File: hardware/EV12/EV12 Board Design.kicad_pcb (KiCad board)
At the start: 4 copper layers, 66 x 99.3 mm, 132 parts, among them CN2 Conn_05x02_Female, CN3 Conn_01x06_Female, CN4 Conn_01x06_Female, CN5 Conn_02x05_Male, CN6 Conn_02x05_Male, CN7 Conn_02x05_Male, J1 Conn_01x02_Socket, J10 Conn_01x08_Socket, J2 AudioJack1, J3 Conn_01x06_Socket, J9 USB_C_Receptacle, Q1 SS8050, Q2 SS8050, SW1 TS-1037-A11B3-D2, SW3 TS-1037-A11B3-D2, SW4 SW_Push, SW5 SW_Push, SW6 SW_SPDT, U1 STM32F405RGTx, U11 ESP32-S3-WROOM-1-N8R2, U13 BM14B(0.8)-24DS-0.4V(53), U2 BQ21040DBV, U3 CH340C, U4 USBLC6-2P6, U5 M24C02-RMN6TP, U6 WM8960CGEFL/RV, U7 TPS63060, U8 STM32F072CBTx, Y1 Crystal_GND24

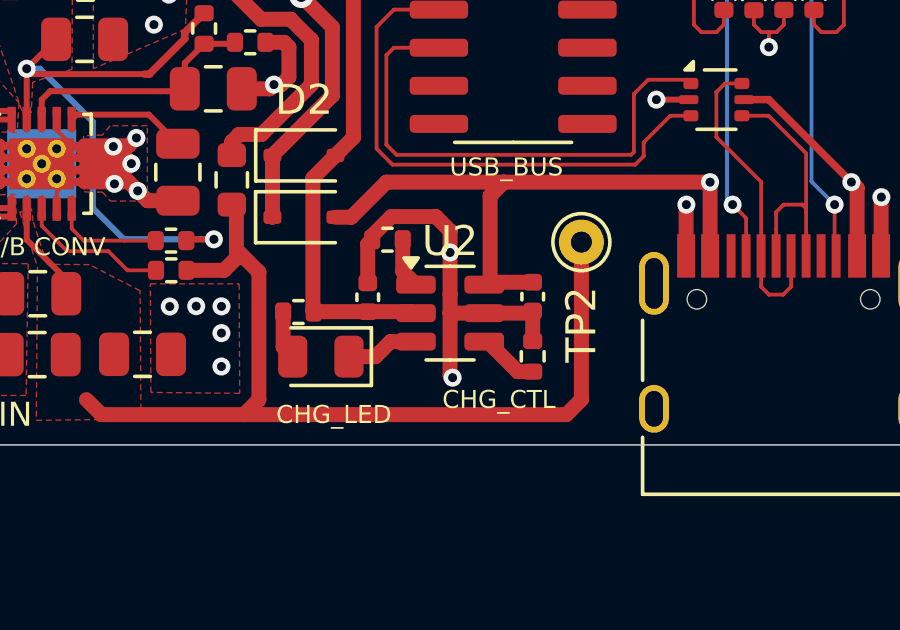
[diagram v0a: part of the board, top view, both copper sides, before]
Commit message: Added missing capacitor to BQ21040DVR battery charger
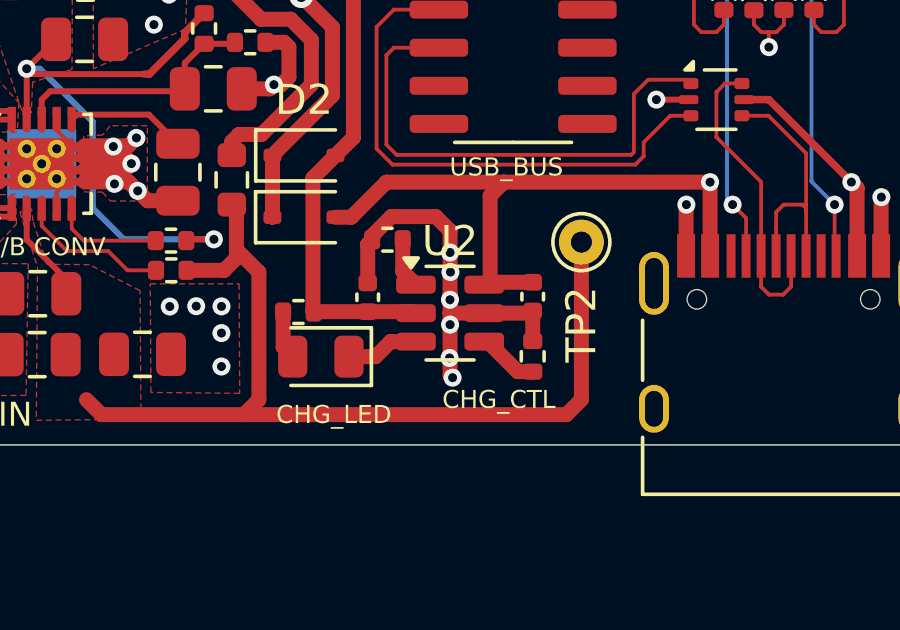
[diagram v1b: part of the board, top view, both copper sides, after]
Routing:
- net GND: vias 71 -> 75
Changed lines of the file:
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@@
 		(tags "resistor")
 		(property "Reference" "R43"
-			(at 0 -1.17 360)
+			(at 0 -1.17 0)
 			(layer "F.SilkS")
 			(hide yes)
@@
 		)
 		(property "Value" "10k"
-			(at 0 1.17 360)
+			(at 0 1.17 0)
 			(layer "F.Fab")
 			(effects
@@
 		)
 		(fp_text user "${REFERENCE}"
-			(at 0 0 360)
+			(at 0 0 0)
 			(layer "F.Fab")
 			(effects
@@
 		(tags "SOT TO_SOT_SMD")
 		(property "Reference" "Q1"
-			(at 0 -2.4 360)
+			(at 0 -2.4 0)
 			(layer "F.SilkS")
 			(hide yes)
@@
 		)
 		(property "Value" "SS8050"
-			(at 0 2.4 360)
+			(at 0 2.4 0)
 			(layer "F.Fab")
 			(effects
@@
 		)
 		(fp_text user "${REFERENCE}"
-			(at 0 0 360)
+			(at 0 0 0)
 			(layer "F.Fab")
 			(effects
@@
 		(tags "SOT TO_SOT_SMD")
 		(property "Reference" "Q2"
-			(at 0 -2.4 360)
+			(at 0 -2.4 0)
 			(layer "F.SilkS")
 			(effects
@@
 		)
 		(property "Value" "SS8050"
-			(at 0 2.4 360)
+			(at 0 2.4 0)
 			(layer "F.Fab")
 			(effects
@@
 		)
 		(fp_text user "${REFERENCE}"
-			(at 0 0 360)
+			(at 0 0 0)
 			(layer "F.Fab")
 			(effects
@@
 		(tags "resistor")
 		(property "Reference" "R28"
-			(at 0.01 0.75 360)
+			(at 0.01 0.75 0)
 			(layer "F.SilkS")
 			(hide yes)
@@
 		)
 		(property "Value" "1k0"
-			(at 0 1.17 360)
+			(at 0 1.17 0)
 			(layer "F.Fab")
 			(effects
@@
 		)
 		(property "Footprint" "Resistor_SMD:R_0402_1005Metric"
-			(at 0 0 360)
+			(at 0 0 0)
 			(layer "F.Fab")
 			(hide yes)
@@
 		)
 		(property "Datasheet" ""
-			(at 0 0 360)
+			(at 0 0 0)
 			(layer "F.Fab")
 			(hide yes)
@@
 		)
 		(property "Description" "Resistor, US symbol"
-			(at 0 0 360)
+			(at 0 0 0)
 			(layer "F.Fab")
 			(hide yes)
@@
 		)
 		(fp_text user "${REFERENCE}"
-			(at 0 0 360)
+			(at 0 0 0)
 			(layer "F.Fab")
 			(effects
@@
 		(tags "resistor")
 		(property "Reference" "R44"
-			(at 0 -1.17 360)
+			(at 0 -1.17 0)
 			(layer "F.SilkS")
 			(hide yes)
@@
 		)
 		(property "Value" "10k"
-			(at 0 1.17 360)
+			(at 0 1.17 0)
 			(layer "F.Fab")
 			(effects
@@
 		)
 		(fp_text user "${REFERENCE}"
-			(at 0 0 360)
+			(at 0 0 0)
 			(layer "F.Fab")
 			(effects
@@
 	)
 	(via
+		(at 135.865743 142.400165)
+		(size 0.6)
+		(drill 0.3)
+		(layers "F.Cu" "B.Cu")
+		(free yes)
+		(net 4)
+	)
+	(via
 		(at 126.26 126.79)
 		(size 0.6)
@@
 	)
 	(via
+		(at 135.8825 141.29)
+		(size 0.6)
+		(drill 0.3)
+		(layers "F.Cu" "B.Cu")
+		(free yes)
+		(net 4)
+	)
+	(via
 		(at 124.657571 135.353492)
 		(size 0.6)
@@
 	)
 	(via
+		(at 135.879657 140.460748)
+		(size 0.6)
+		(drill 0.3)
+		(layers "F.Cu" "B.Cu")
+		(free yes)
+		(net 4)
+	)
+	(via
 		(at 170.76 102.04)
 		(size 0.6)
@@
 		(net 4)
 	)
+	(via
+		(at 135.894594 139.53812)
+		(size 0.6)
+		(drill 0.3)
+		(layers "F.Cu" "B.Cu")
+		(free yes)
+		(net 4)
+	)

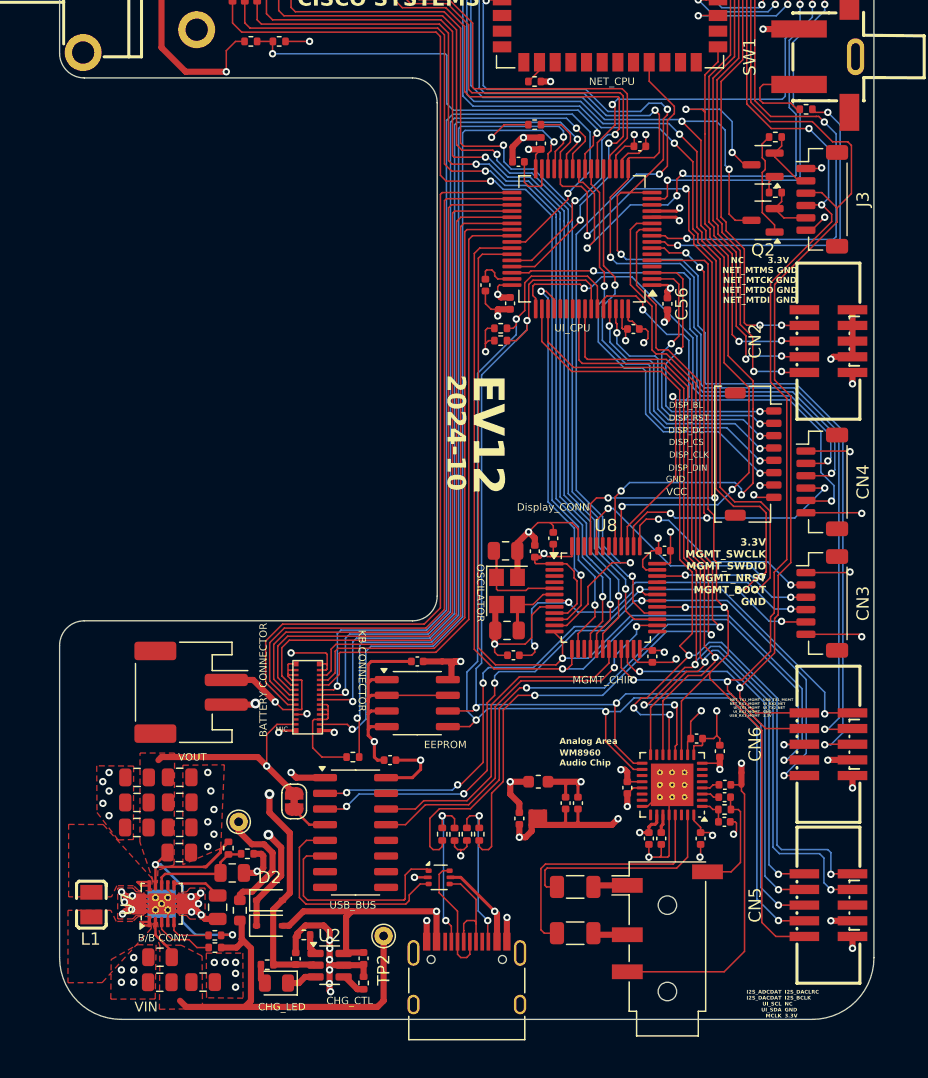
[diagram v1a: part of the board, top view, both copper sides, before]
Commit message: Moved keyboard conn, eeprom, and battery connector. Added diodes
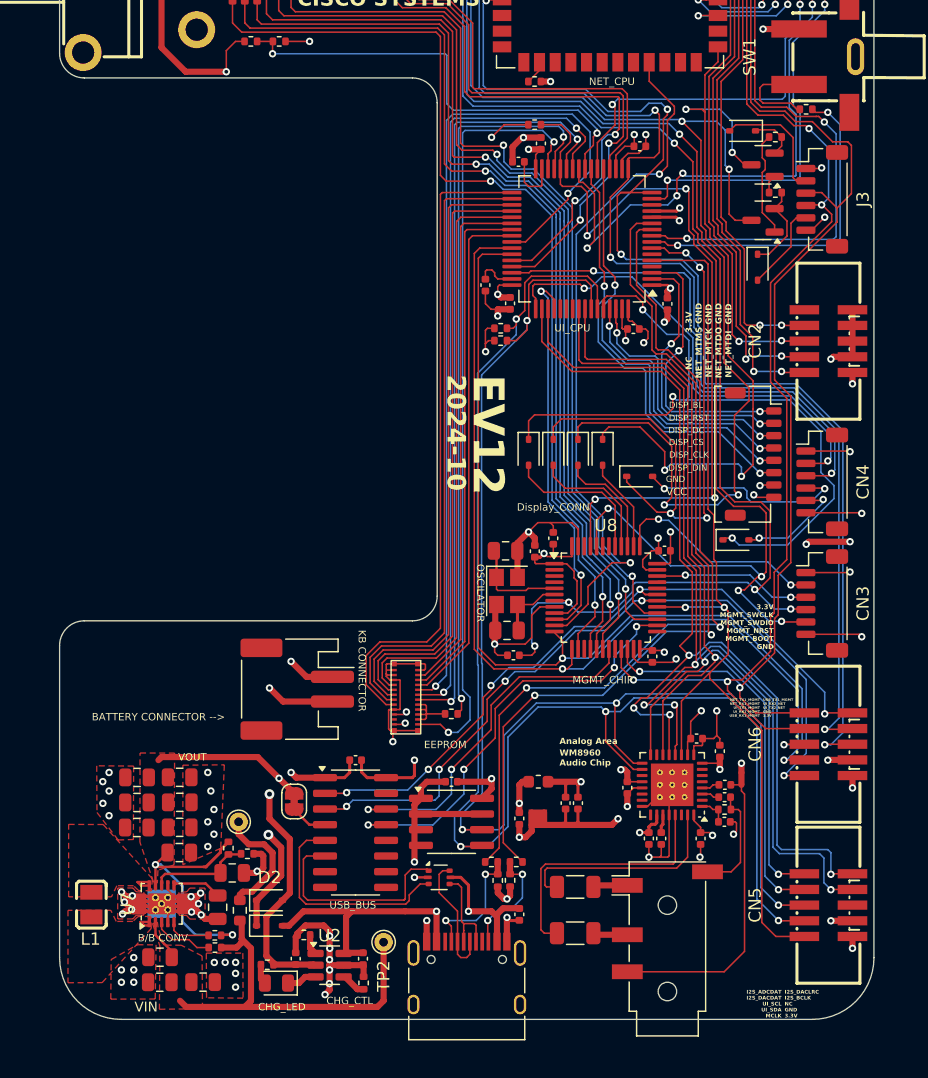
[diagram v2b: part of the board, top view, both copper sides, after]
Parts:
- added C21: 10u, Capacitor_SMD:C_0402_1005Metric, F.Cu at (138.6, 140.4)
- added D10: 1N5819WS, Diode_SMD:D_SOD-323, F.Cu at (170.6, 84.3)
- added D11: 1N5819WS, Diode_SMD:D_SOD-323, F.Cu at (169.4, 73.3)
- added D12: 1N5819WS, Diode_SMD:D_SOD-323, F.Cu at (158.0, 99.3)
- added D13: 1N5819WS, Diode_SMD:D_SOD-323, F.Cu at (156.0, 99.3)
- added D14: 1N5819WS, Diode_SMD:D_SOD-323, F.Cu at (168.8, 106.4)
- added D15: 1N5819WS, Diode_SMD:D_SOD-323, F.Cu at (161.0, 101.3)
- added D8: 1N5819WS, Diode_SMD:D_SOD-323, F.Cu at (154.0, 99.3)
- added D9: 1N5819WS, Diode_SMD:D_SOD-323, F.Cu at (152.0, 99.3)
- moved C1 13.1 mm to (151.3, 136.8)
- moved C20 10.1 mm to (145.8, 126.0)
- moved U5 10.0 mm to (145.8, 129.3)
- moved R30 8.71 mm to (145.8, 120.5)
- moved J1 8.60 mm to (133.3, 118.5)
- moved U13 7.96 mm to (143.3, 122.2)
- moved R2 5.12 mm to (150.5, 134.0)
- moved R3 5.12 mm to (149.5, 134.0)
- moved R31 4.58 mm to (149.0, 132.5), turned to 0 degrees
- moved R33 3.75 mm to (151.0, 132.5), turned to 180 degrees
- moved C32 2.79 mm to (138.0, 124.3)
- moved TP2 0.50 mm to (140.3, 139.0)
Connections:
- CN4 pad 4: /UI_NRST -> Net-(CN4-Pin_4)
- CN4 pad 5: /UI_BOOT0 -> Net-(CN4-Pin_5)
- Q1 pad 2: /NET_DTR -> Net-(D11-K)
- Q2 pad 2: /NET_RTS -> Net-(D10-K)
- R43 pad 1: /NET_RTS -> Net-(D10-K)
- R44 pad 1: /NET_DTR -> Net-(D11-K)
- U8 pad 38: /UI_NRST -> Net-(D12-A)
- U8 pad 39: /UI_BOOT0 -> Net-(D13-A)
- U8 pad 40: /NET_NRST -> Net-(D8-A)
- U8 pad 41: /NET_BOOT -> Net-(D9-A)
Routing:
- net /UI_SDA: track 99.1 -> 119.4 mm
- net /UI_SCL: track 96.3 -> 116.0 mm
- net Net-(CN4-Pin_4): track 0.00 -> 17.2 mm, vias 0 -> 2
- net +3.3V: track 483.2 -> 497.3 mm, vias 31 -> 34
- net Net-(D9-A): track 0.00 -> 12.2 mm
- net Net-(D8-A): track 0.00 -> 10.7 mm
- net Net-(U1-PB10): track 69.8 -> 59.8 mm
- net /UI_BOOT0: track 49.9 -> 59.0 mm
- net Net-(D13-A): track 0.00 -> 9.15 mm
- net Net-(CN4-Pin_5): track 0.00 -> 9.03 mm, vias 0 -> 2
- net /NET_NRST: track 101.9 -> 110.4 mm
- net GNDA: track 78.6 -> 70.7 mm
- net /KB_ROW1: track 61.2 -> 53.3 mm
- net /KB_COL4: track 50.3 -> 42.4 mm
- net /KB_ROW3: track 50.1 -> 42.2 mm
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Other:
- board text added: "BATTERY CONNECTOR -->"
- board text added: "KEEP OUT BATTERY CONNECTOR WILL BE IN THIS PATH"
- board text removed: "BATTERY CONNECTOR"
- board text removed: "MIC"

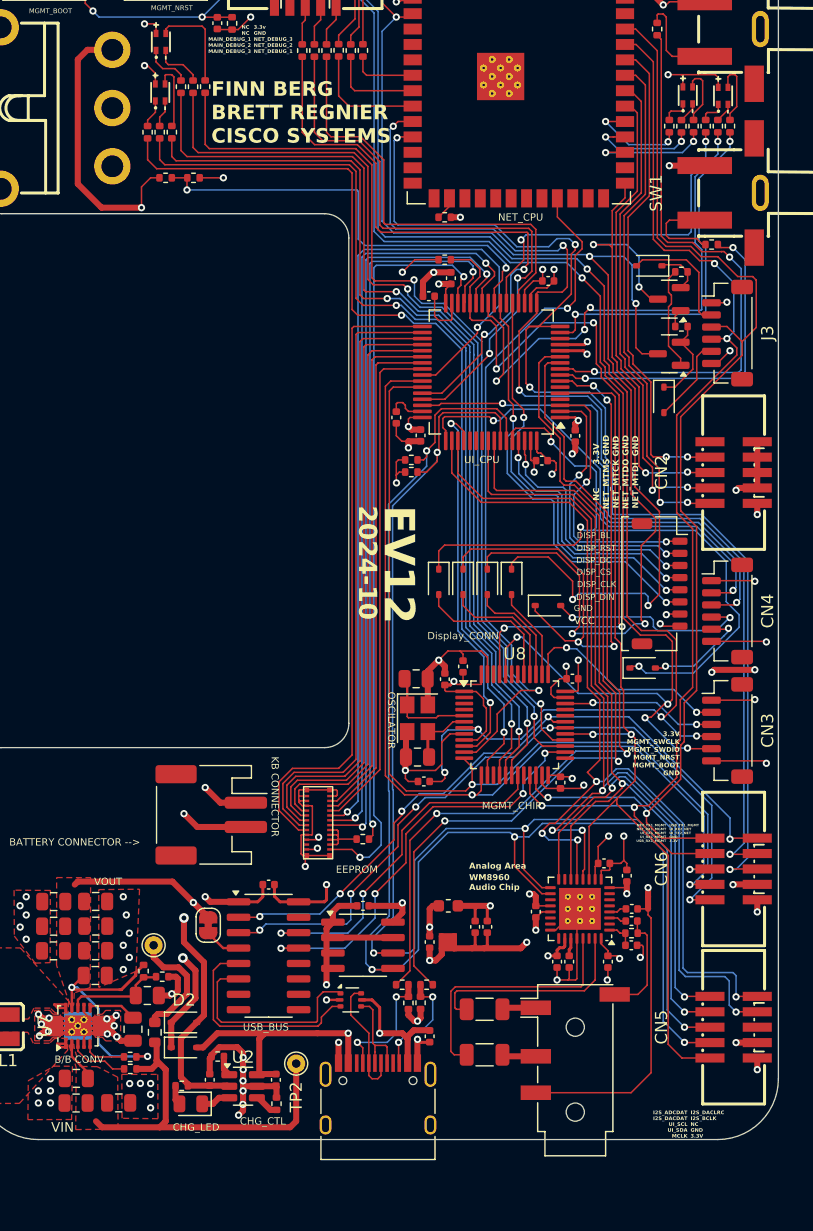
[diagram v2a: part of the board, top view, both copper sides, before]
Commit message: Removed diodes and auto reset circuit
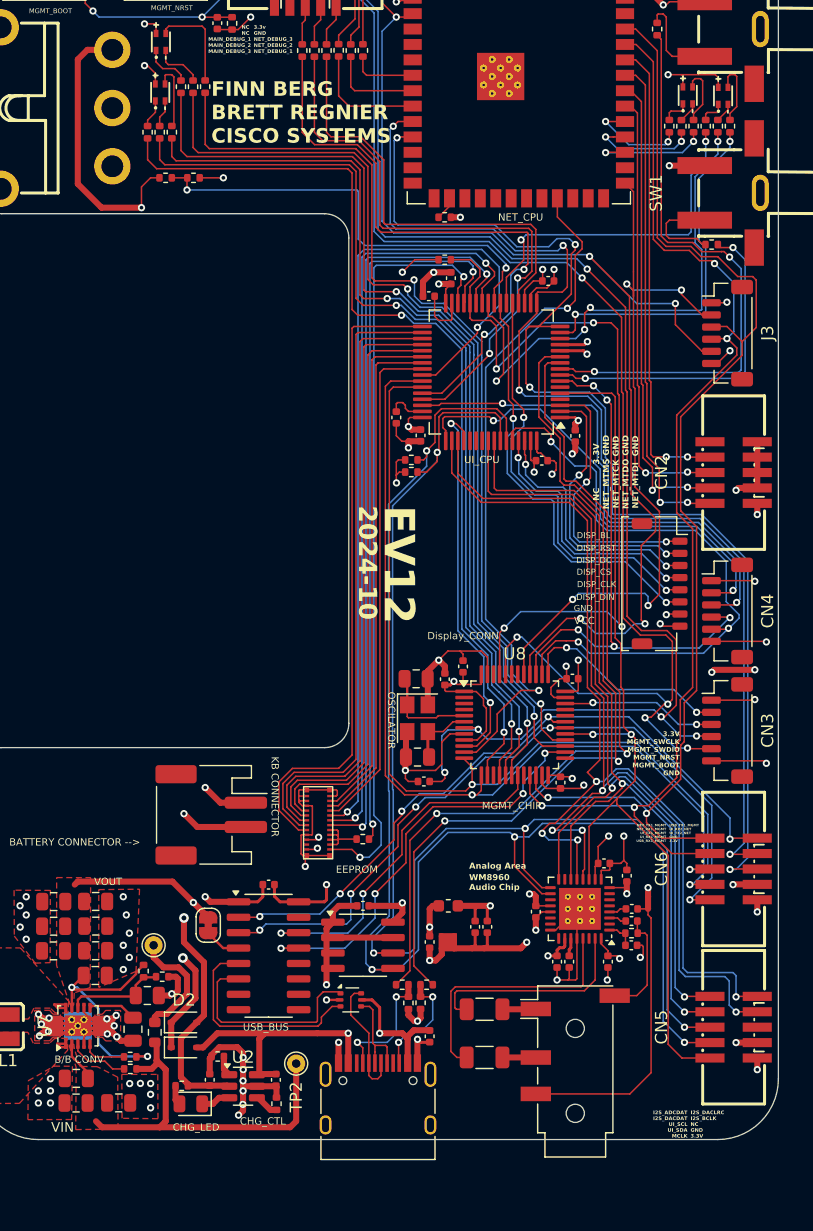
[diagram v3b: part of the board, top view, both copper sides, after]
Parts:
- removed D10, D11, D12, D13, D14, D15, D8, D9: 1N5819WS, Diode_SMD:D_SOD-323
- removed Q1, Q2: SS8050, Package_TO_SOT_SMD:SOT-23
- removed R43, R44: 10k, Resistor_SMD:R_0402_1005Metric
- moved C29 0.22 mm to (155.8, 138.5)
- moved J2 0.10 mm to (163.3, 138.4)
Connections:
- CN4 pad 4: Net-(CN4-Pin_4) -> /UI_NRST
- CN4 pad 5: Net-(CN4-Pin_5) -> /UI_BOOT0
- J3 pad 2: /NET_DTR -> /NET_BOOT
- J3 pad 5: /NET_RTS -> /NET_NRST
- U8 pad 38: Net-(D12-A) -> /UI_BOOT0
- U8 pad 39: Net-(D13-A) -> /UI_NRST
- U8 pad 40: Net-(D8-A) -> /NET_NRST
- U8 pad 41: Net-(D9-A) -> /NET_BOOT
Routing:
- net Net-(CN4-Pin_4): track 17.2 -> 0.00 mm, vias 2 -> 0
- net Net-(D9-A): track 12.2 -> 0.00 mm
- net Net-(D8-A): track 10.7 -> 0.00 mm
- net /NET_DTR: track 10.2 -> 0.00 mm
- net Net-(D13-A): track 9.15 -> 0.00 mm
- net Net-(CN4-Pin_5): track 9.03 -> 0.00 mm, vias 2 -> 0
- net Net-(Q2-B): track 8.54 -> 0.00 mm
- net Net-(D12-A): track 7.61 -> 0.00 mm
- net Net-(D10-K): track 7.17 -> 0.00 mm
- net /NET_RTS: track 7.13 -> 0.00 mm
- net /UI_BOOT0: track 59.0 -> 52.3 mm
- net /NET_NRST: track 110.4 -> 104.2 mm
- net /UI_NRST: track 51.1 -> 46.7 mm, vias 4 -> 5
- net Net-(D11-K): track 3.97 -> 0.00 mm
- net /NET_BOOT: track 62.9 -> 60.9 mm
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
